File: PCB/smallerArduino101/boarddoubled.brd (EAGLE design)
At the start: 47.9 x 59.7 mm, 41 parts

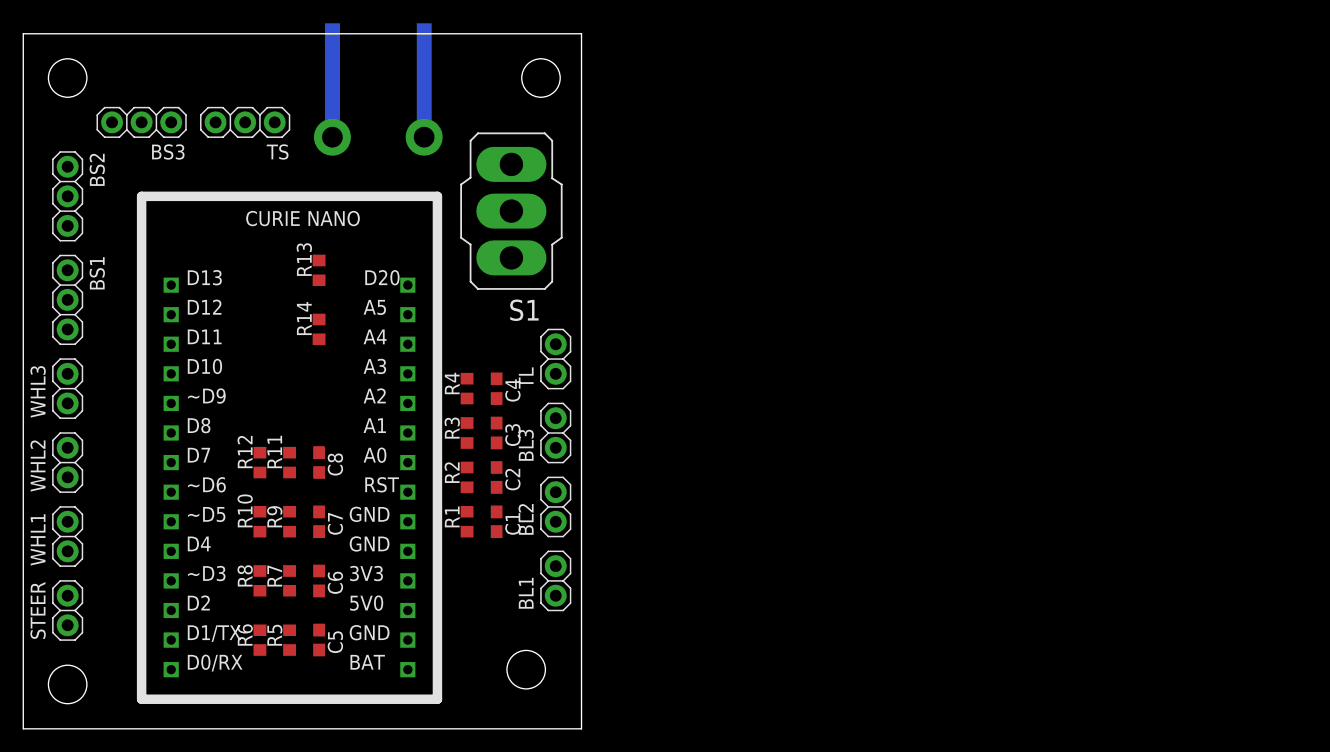
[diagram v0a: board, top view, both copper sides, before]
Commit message: finshed routing, made a board with duplicate, need to check anderson
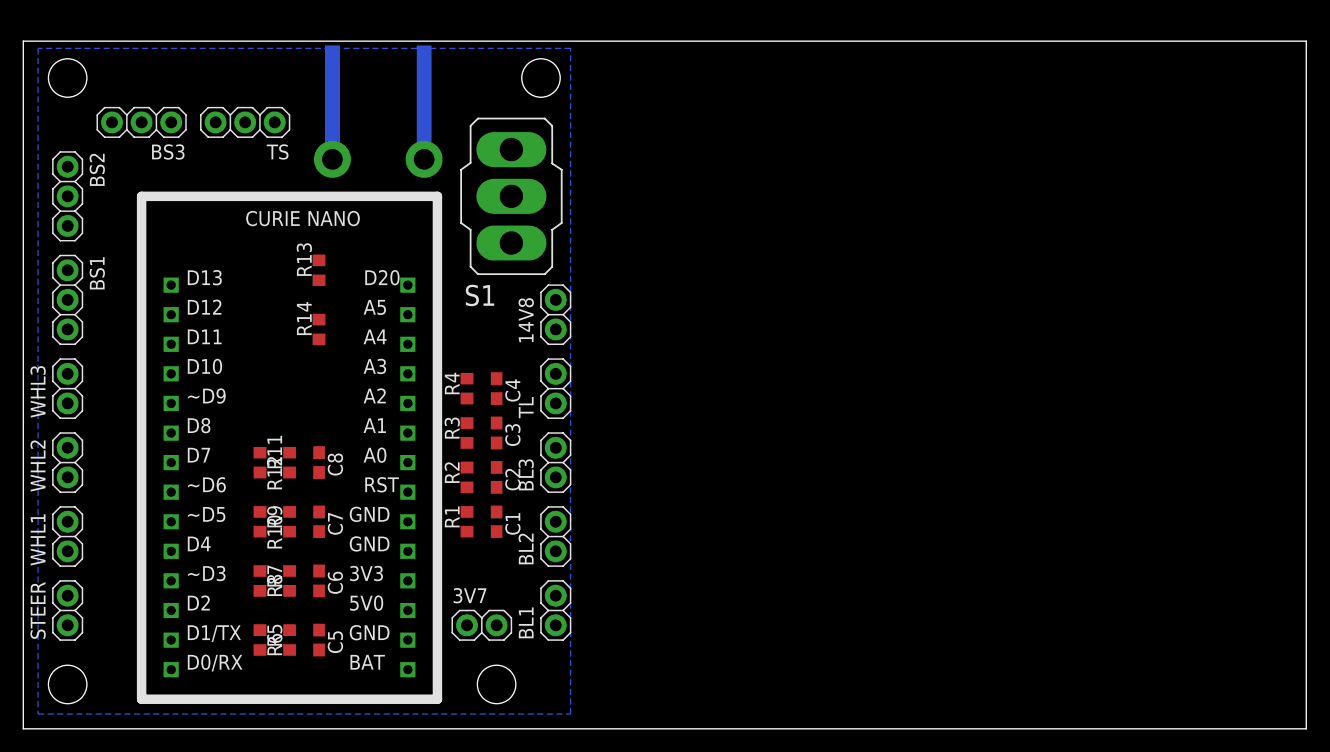
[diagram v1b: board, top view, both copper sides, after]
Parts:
- added 3V7: (no value), ee192:1X02
- added LIPO: ANDERSONHORIZONTAL, ee192:ANDERSON_HORIZONTAL
- 14V8: value ANDERSONHORIZONTAL -> (none); device ee192:ANDERSON_HORIZONTAL -> ee192:1X02
- moved 14V8 21.6 mm to (66.0, 35.6), flipped to the top, turned to 90 degrees
- moved JP14 2.84 mm to (61.0, 3.81)
- moved BL1 2.54 mm to (66.0, 10.2)
- moved BL2 2.54 mm to (66.0, 16.5)
- moved BL3 2.54 mm to (66.0, 22.9)
- moved TL 2.54 mm to (66.0, 29.2)
- moved S1 1.27 mm to (62.2, 45.7)
- turned R10 to 270 degrees
- turned R12 to 270 degrees
- turned R6 to 270 degrees
- turned R8 to 270 degrees
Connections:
- net 14V8: now also 14V8.2
- net 3V7: now also 3V7.2
- net GND: now also 14V8.1, 3V7.1, LIPO.PIN1, LIPO.PIN1-LEAD; no longer 14V8.PIN1, 14V8.PIN1-LEAD
- net N$5: now also LIPO.PIN2, LIPO.PIN2-LEAD; no longer 14V8.PIN2, 14V8.PIN2-LEAD
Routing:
- added copper zone on layer 16, net GND
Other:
- board size 47.9 x 59.7 mm -> 110.2 x 59 mm

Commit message: submitted ersion of gerber to bac
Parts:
- added 14V1, 3V1, BL4, BL5, BL6, STEER1, TL1, WHL4, WHL5, WHL6: (no value), ee192:1X02
- added BS4, BS5, BS6, TS1: (no value), ee192:1X03
- added C10, C11, C12, C9: 0.1u, adafruit:C0603
- added C13, C14, C15, C16: 1n, adafruit:C0603
- added JP1, JP2, JP3, JP4: STAND-OFF, ee192:STAND-OFF
- added LIPO1: ANDERSONHORIZONTAL, ee192:ANDERSON_HORIZONTAL
- added R15, R21, R22, R23: 5.1k, resistor:R0603
- added R16, R17, R18, R28: 1k, resistor:R0603
- added R19: 10K, resistor:R0603
- added R20: 1K, resistor:R0603
- added R24, R25, R26, R27: 10k, resistor:R0603
- added S2: (no value), switch:320-916
- added U$2: CURIENANO_BREAKOUT, Curie Nano:CURIENANO
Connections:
- new net 14V1: 14V1.2, BS4.1, BS5.1, BS6.1, R19.2, S2.1, TS1.1
- new net 3V1: 3V1.2, U$2.BAT
- new net 3V2: BL4.2, BL5.2, BL6.2, STEER1.2, TL1.2, U$2.3V3, WHL4.2, WHL5.2, WHL6.2
- new net BAT_CHECK1: R19.1, R20.2, U$2.A4
- new net BRAKE_P4: BL4.1, C9.1, R15.2, U$2.A0
- new net BRAKE_P5: BL5.1, C10.1, R21.2, U$2.A1
- new net BRAKE_P6: BL6.1, C11.1, R22.2, U$2.A2
- new net BRAKE_PWM4: BS5.3, U$2.D11
- new net BRAKE_PWM5: BS4.3, U$2.D10
- new net BRAKE_PWM6: BS6.3, U$2.~D9
- new net GND1: 14V1.1, 3V1.1, BS4.2, BS5.2, BS6.2, C10.2, C11.2, C12.2, C13.2, C14.2, C15.2, C16.2, C9.2, LIPO1.PIN1, LIPO1.PIN1-LEAD, R15.1, R20.1, R21.1, R22.1, R23.1, R24.1, R25.1, R26.1, R27.1, TS1.2, U$2.GND3
- new net N$10: LIPO1.PIN2, LIPO1.PIN2-LEAD, S2.2
- new net N$6: R28.2, STEER1.1
- new net N$7: R16.2, WHL4.1
- new net N$8: R17.2, WHL5.1
- new net N$9: R18.2, WHL6.1
- new net STEERING_P1: C13.1, R24.2, R28.1, U$2.~D5
- new net TILT_P1: C12.1, R23.2, TL1.1, U$2.A3
- new net TILT_PWM1: TS1.3, U$2.D12
- new net WHEEL_P4: C16.1, R18.1, R27.2, U$2.D8
- new net WHEEL_P5: C15.1, R17.1, R26.2, U$2.D7
- new net WHEEL_P6: C14.1, R16.1, R25.2, U$2.~D6
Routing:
- net 3V2: track 0.00 -> 107.7 mm
- net 3V3: track 0.00 -> 107.7 mm
- net 14V8: track 0.00 -> 67.6 mm
- net 14V1: track 0.00 -> 67.6 mm
- net N$7: track 0.00 -> 43.8 mm
- net N$2: track 0.00 -> 43.8 mm
- net N$8: track 0.00 -> 41.1 mm
- net N$3: track 0.00 -> 41.1 mm
- net GND1: track 0.00 -> 33.5 mm, vias 0 -> 9
- net GND: track 0.00 -> 33.5 mm, vias 0 -> 9
- net N$9: track 0.00 -> 28.8 mm
- net N$4: track 0.00 -> 28.8 mm
- net BRAKE_PWM3: track 0.00 -> 21.7 mm, vias 0 -> 1
- net BRAKE_PWM4: track 0.00 -> 21.7 mm, vias 0 -> 1
- net BRAKE_P4: track 0.00 -> 21.6 mm
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- added copper zone on layer 16, net GND1
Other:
- board size 110.2 x 59 mm -> 98.7 x 59 mm
